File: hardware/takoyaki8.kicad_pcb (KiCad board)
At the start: 2 copper layers, 0 parts

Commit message: Place parts on first-draft layout: outline with RP2040-Zero notch, mounting holes, OLED silk outline removed (DRC clean except silk text)
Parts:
- added C1: 100nF, Capacitor_SMD:C_0603_1608Metric, B.Cu at (133.5, 85.8)
- added C2: 100nF, Capacitor_SMD:C_0603_1608Metric, B.Cu at (152.6, 85.8)
- added C3: 100nF, Capacitor_SMD:C_0603_1608Metric, B.Cu at (171.6, 85.8)
- added C4: 100nF, Capacitor_SMD:C_0603_1608Metric, B.Cu at (190.7, 85.8)
- added D1: 1N4148W, Diode_SMD:D_SOD-123, B.Cu at (140.5, 75.5)
- added D2: 1N4148W, Diode_SMD:D_SOD-123, B.Cu at (159.6, 75.5)
- added D3: 1N4148W, Diode_SMD:D_SOD-123, B.Cu at (178.6, 75.5)
- added D4: 1N4148W, Diode_SMD:D_SOD-123, B.Cu at (197.7, 75.5)
- added D5: 1N4148W, Diode_SMD:D_SOD-123, B.Cu at (140.5, 94.5)
- added D6: 1N4148W, Diode_SMD:D_SOD-123, B.Cu at (159.6, 94.5)
- added D7: 1N4148W, Diode_SMD:D_SOD-123, B.Cu at (178.6, 94.5)
- added D8: 1N4148W, Diode_SMD:D_SOD-123, B.Cu at (197.7, 94.5)
- added J1: OLED_0.91in, takoyaki8:OLED_0.91in_I2C_Header, F.Cu at (117.4, 97.2)
- added LED1: WS2812B, LED_SMD:LED_WS2812B_PLCC4_5.0x5.0mm_P3.2mm, B.Cu at (133.5, 82.0)
- added LED2: WS2812B, LED_SMD:LED_WS2812B_PLCC4_5.0x5.0mm_P3.2mm, B.Cu at (152.6, 82.0)
- added LED3: WS2812B, LED_SMD:LED_WS2812B_PLCC4_5.0x5.0mm_P3.2mm, B.Cu at (171.6, 82.0)
- added LED4: WS2812B, LED_SMD:LED_WS2812B_PLCC4_5.0x5.0mm_P3.2mm, B.Cu at (190.7, 82.0)
- added R1: 0R, Resistor_SMD:R_0603_1608Metric, B.Cu at (128.0, 80.3)
- added SW1: SW_Push, takoyaki8:SW_choc_v2_HS_CPG135001S30_1u, B.Cu at (133.5, 70.5)
- added SW2: SW_Push, takoyaki8:SW_choc_v2_HS_CPG135001S30_1u, B.Cu at (152.6, 70.5)
- added SW3: SW_Push, takoyaki8:SW_choc_v2_HS_CPG135001S30_1u, B.Cu at (171.6, 70.5)
- added SW4: SW_Push, takoyaki8:SW_choc_v2_HS_CPG135001S30_1u, B.Cu at (190.7, 70.5)
- added SW5: SW_Push, takoyaki8:SW_choc_v2_HS_CPG135001S30_1u, B.Cu at (133.5, 89.5)
- added SW6: SW_Push, takoyaki8:SW_choc_v2_HS_CPG135001S30_1u, B.Cu at (152.6, 89.5)
- added SW7: SW_Push, takoyaki8:SW_choc_v2_HS_CPG135001S30_1u, B.Cu at (171.6, 89.5)
- added SW8: SW_Push, takoyaki8:SW_choc_v2_HS_CPG135001S30_1u, B.Cu at (190.7, 89.5)
- added U1: RP2040-Zero, takoyaki8:RP2040-Zero_Castellated_Flipped, F.Cu at (113.6, 71.9)
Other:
- board outline added: 99.9 x 40 mm

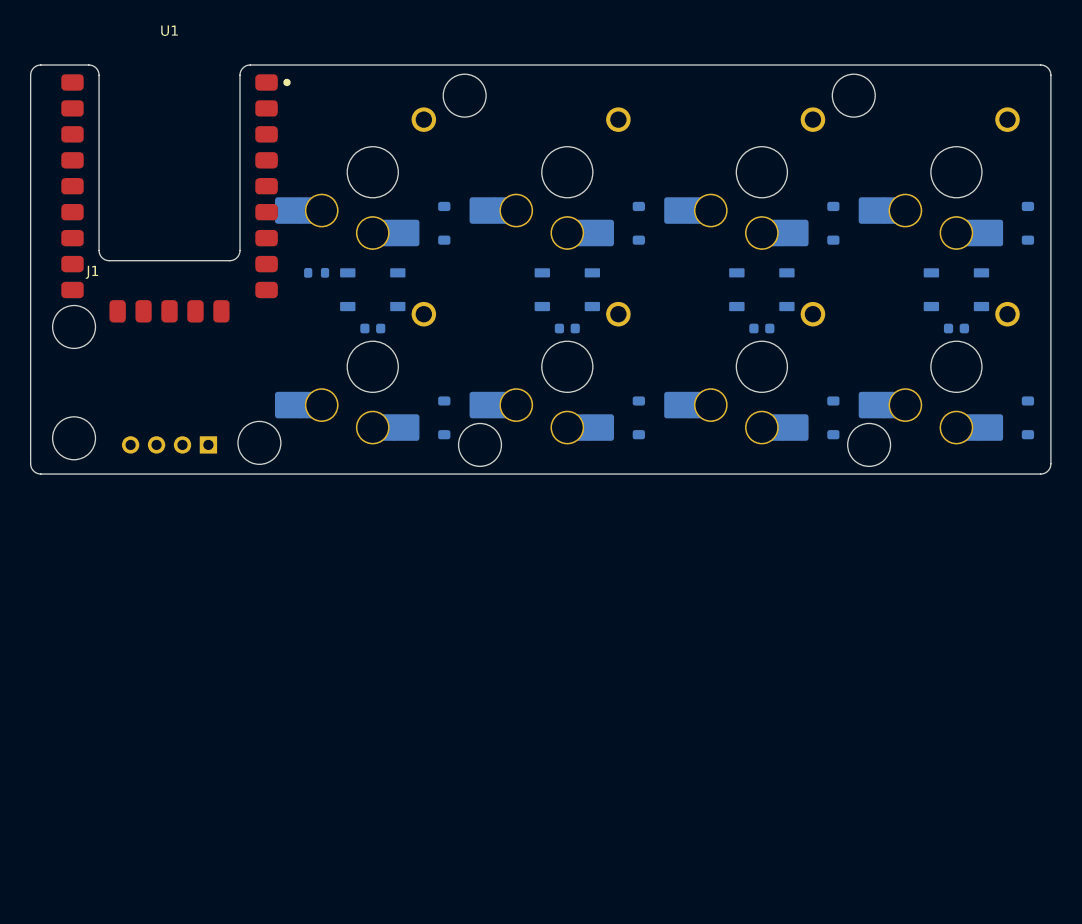
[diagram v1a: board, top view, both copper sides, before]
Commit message: Add top plate, panel tabs and mouse-bite holes (DRC clean except silk text)
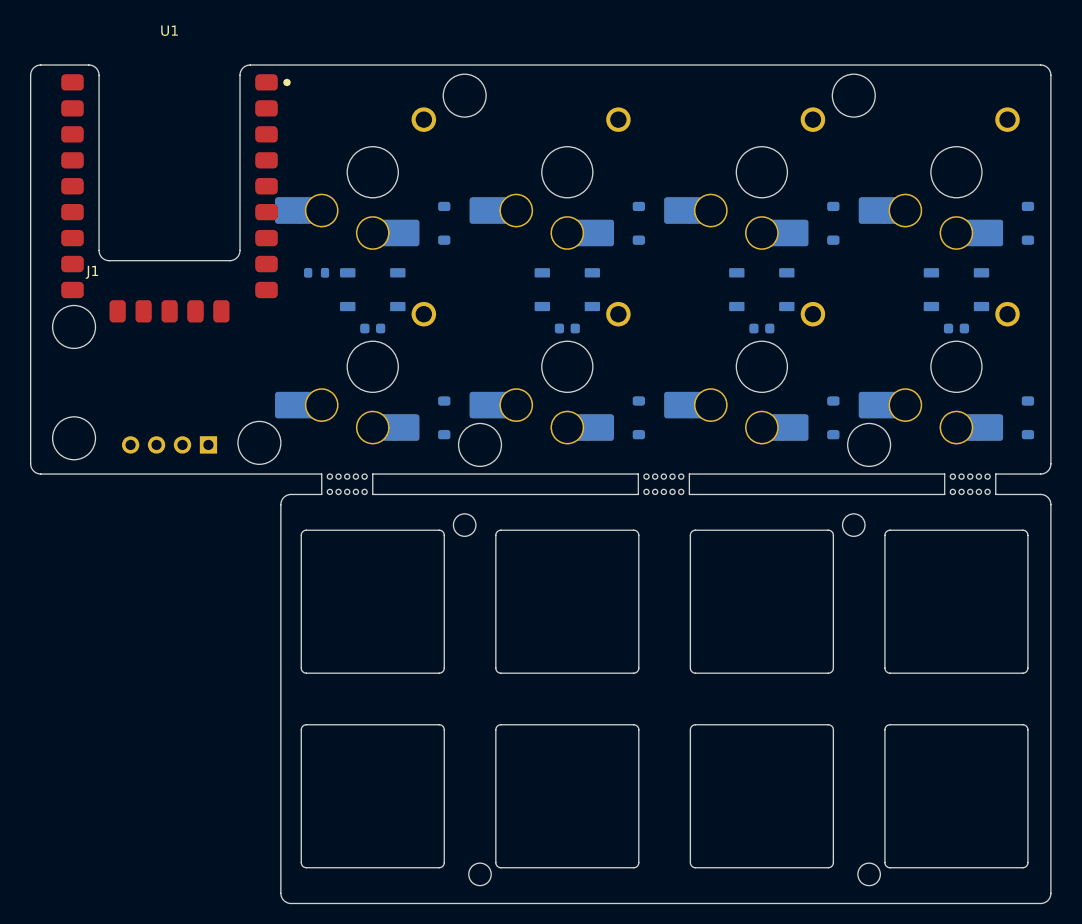
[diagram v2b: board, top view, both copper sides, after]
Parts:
- added MB1: MouseBite, takoyaki8:MouseBite_5x0.5mm_P0.85mm, F.Cu at (131.0, 100.3)
- added MB2: MouseBite, takoyaki8:MouseBite_5x0.5mm_P0.85mm, F.Cu at (131.0, 101.8)
- added MB3: MouseBite, takoyaki8:MouseBite_5x0.5mm_P0.85mm, F.Cu at (162.0, 100.3)
- added MB4: MouseBite, takoyaki8:MouseBite_5x0.5mm_P0.85mm, F.Cu at (162.0, 101.8)
- added MB5: MouseBite, takoyaki8:MouseBite_5x0.5mm_P0.85mm, F.Cu at (192.0, 100.3)
- added MB6: MouseBite, takoyaki8:MouseBite_5x0.5mm_P0.85mm, F.Cu at (192.0, 101.8)
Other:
- board size 99.9 x 40 mm -> 99.9 x 82.1 mm

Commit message: Add GND zones on both layers, Power netclass, hole-to-hole 0.5mm (DRC: 0 errors, 40 unconnected, 24 mouse-bite hole warnings)
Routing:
- added copper zone on B.Cu, net GND
- added copper zone on F.Cu, net GND
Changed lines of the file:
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@@
 		(capping no)
 		(filling no)
+		(zone_defaults)
 		(pcbplotparams
 			(layerselection 0x00000000_00000000_55555555_5755f5ff)
@@
 		(layer "Edge.Cuts")
 	)
+	(zone
+		(net "GND")
+		(layers "F.Cu" "B.Cu")
+		(hatch edge 0.5)
+		(connect_pads
+			(clearance 0.2)
+		)
+		(min_thickness 0.25)
+		(fill yes
+			(thermal_gap 0.3)
+			(thermal_bridge_width 0.4)
+			(island_removal_mode 0)
+		)
+		(polygon
+			(pts
+				(xy 99.05 59) (xy 200.95 59) (xy 200.9 99.55) (xy 99 99.55)
+			)
+		)
+	)
 	(embedded_fonts no)

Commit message: Route +5V: U1 to LEDs and bypass caps (DRC: 0 errors, 32 unconnected)
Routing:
- net +5V: track 0.00 -> 121.2 mm, vias 0 -> 1
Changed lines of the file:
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@@
 		)
+	)
+	(segment
+		(start 123.1 61.71)
+		(end 126 61.71)
+		(width 0.5)
+		(layer "F.Cu")
+		(net "+5V")
+	)
+	(segment
+		(start 126 61.71)
+		(end 126 79)
+		(width 0.5)
+		(layer "F.Cu")
+		(net "+5V")
+	)
+	(segment
+		(start 126 79)
+		(end 135.95 79)
+		(width 0.5)
+		(layer "B.Cu")
+		(net "+5V")
+	)
+	(segment
+		(start 135.95 79)
+		(end 155 79)
+		(width 0.5)
+		(layer "B.Cu")
+		(net "+5V")
+	)
+	(segment
+		(start 155 79)
+		(end 174.05 79)
+		(width 0.5)
+		(layer "B.Cu")
+		(net "+5V")
+	)
+	(segment
+		(start 174.05 79)
+		(end 193.1 79)
+		(width 0.5)
+		(layer "B.Cu")
+		(net "+5V")
+	)
+	(segment
+		(start 135.95 79)
+		(end 135.95 80.35)
+		(width 0.5)
+		(layer "B.Cu")
+		(net "+5V")
+	)
+	(segment
+		(start 155 79)
+		(end 155 80.35)
+		(width 0.5)
+		(layer "B.Cu")
+		(net "+5V")
+	)
+	(segment
+		(start 174.05 79)
+		(end 174.05 80.35)
+		(width 0.5)
+		(layer "B.Cu")
+		(net "+5V")
+	)
+	(segment
+		(start 193.1 79)
+		(end 193.1 80.35)
+		(width 0.5)
+		(layer "B.Cu")
+		(net "+5V")
+	)
+	(segment
+		(start 134.275 85.8)
+		(end 134.275 80.35)
+		(width 0.5)
+		(layer "B.Cu")
+		(net "+5V")
+	)
+	(segment
+		(start 134.275 80.35)
+		(end 135.95 80.35)
+		(width 0.5)
+		(layer "B.Cu")
+		(net "+5V")
+	)
+	(segment
+		(start 153.325 85.8)
+		(end 153.325 80.35)
+		(width 0.5)
+		(layer "B.Cu")
+		(net "+5V")
+	)
+	(segment
+		(start 153.325 80.35)
+		(end 155 80.35)
+		(width 0.5)
+		(layer "B.Cu")
+		(net "+5V")
+	)
+	(segment
+		(start 172.375 85.8)
+		(end 172.375 80.35)
+		(width 0.5)
+		(layer "B.Cu")
+		(net "+5V")
+	)
+	(segment
+		(start 172.375 80.35)
+		(end 174.05 80.35)
+		(width 0.5)
+		(layer "B.Cu")
+		(net "+5V")
+	)
+	(segment
+		(start 191.425 85.8)
+		(end 191.425 80.35)
+		(width 0.5)
+		(layer "B.Cu")
+		(net "+5V")
+	)
+	(segment
+		(start 191.425 80.35)
+		(end 193.1 80.35)
+		(width 0.5)
+		(layer "B.Cu")
+		(net "+5V")
+	)
+	(via
+		(at 126 79)
+		(size 0.6)
+		(drill 0.3)
+		(layers "F.Cu" "B.Cu")
+		(net "+5V")
 	)
 	(embedded_fonts no)

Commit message: Route LED data chain (GPIO26 -> R1 -> LED1..4) and chamfer +5V corners (DRC: 0 errors, 27 unconnected)
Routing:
- net LED_D1: track 0.00 -> 16.9 mm
- net LED_D2: track 0.00 -> 16.9 mm
- net LED_D3: track 0.00 -> 16.9 mm
- net LED_DATA: track 0.00 -> 7.18 mm, vias 0 -> 1
- net Net-(LED1-DIN): track 0.00 -> 2.23 mm
- net +5V: track 121.2 -> 119.7 mm
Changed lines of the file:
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@@
 		(capping no)
 		(filling no)
-		(zone_defaults)
 		(pcbplotparams
 			(layerselection 0x00000000_00000000_55555555_5755f5ff)
@@
 		(layer "Edge.Cuts")
 	)
-	(zone
-		(net "GND")
-		(layers "F.Cu" "B.Cu")
-		(hatch edge 0.5)
-		(connect_pads
-			(clearance 0.2)
-		)
-		(min_thickness 0.25)
-		(fill yes
-			(thermal_gap 0.3)
-			(thermal_bridge_width 0.4)
-			(island_removal_mode 0)
-		)
-		(polygon
-			(pts
-				(xy 99.05 59) (xy 200.95 59) (xy 200.9 99.55) (xy 99 99.55)
-			)
-		)
+	(segment
+		(start 126 62.21)
+		(end 126 79)
+		(width 0.5)
+		(layer "F.Cu")
+		(net "+5V")
 	)
 	(segment
-		(start 123.1 61.71)
-		(end 126 61.71)
+		(start 125.5 61.71)
+		(end 126 62.21)
 		(width 0.5)
 		(layer "F.Cu")
@@
 	)
 	(segment
-		(start 126 61.71)
-		(end 126 79)
+		(start 123.1 61.71)
+		(end 125.5 61.71)
 		(width 0.5)
 		(layer "F.Cu")
 		(net "+5V")
 	)
+	(via
+		(at 126 79)
+		(size 0.6)
+		(drill 0.3)
+		(layers "F.Cu" "B.Cu")
+		(net "+5V")
+	)
+	(segment
+		(start 134.775 80.35)
+		(end 135.95 80.35)
+		(width 0.5)
+		(layer "B.Cu")
+		(net "+5V")
+	)
+	(segment
+		(start 191.925 80.35)
+		(end 193.1 80.35)
+		(width 0.5)
+		(layer "B.Cu")
+		(net "+5V")
+	)
+	(segment
+		(start 153.325 80.85)
+		(end 153.825 80.35)
+		(width 0.5)
+		(layer "B.Cu")
+		(net "+5V")
+	)
 	(segment
 		(start 126 79)
@@
 	)
 	(segment
-		(start 135.95 79)
-		(end 155 79)
+		(start 153.825 80.35)
+		(end 155 80.35)
 		(width 0.5)
 		(layer "B.Cu")
@@
 	)
 	(segment
-		(start 155 79)
-		(end 174.05 79)
+		(start 193.1 79)
+		(end 193.1 80.35)
 		(width 0.5)
 		(layer "B.Cu")
@@
 	)
 	(segment
-		(start 174.05 79)
-		(end 193.1 79)
+		(start 172.375 85.8)
+		(end 172.375 80.85)
+		(width 0.5)
+		(layer "B.Cu")
+		(net "+5V")
+	)
+	(segment
+		(start 172.375 80.85)
+		(end 172.875 80.35)
 		(width 0.5)
 		(layer "B.Cu")
@@
 	)
 	(segment
-		(start 155 79)
-		(end 155 80.35)
+		(start 172.875 80.35)
+		(end 174.05 80.35)
+		(width 0.5)
+		(layer "B.Cu")
+		(net "+5V")
+	)
+	(segment
+		(start 191.425 85.8)
+		(end 191.425 80.85)
 		(width 0.5)
 		(layer "B.Cu")
@@
 	)
 	(segment
-		(start 193.1 79)
-		(end 193.1 80.35)
+		(start 135.95 79)
+		(end 155 79)
 		(width 0.5)
 		(layer "B.Cu")
@@
 	(segment
 		(start 134.275 85.8)
-		(end 134.275 80.35)
+		(end 134.275 80.85)
 		(width 0.5)
 		(layer "B.Cu")
@@
 	)
 	(segment
-		(start 134.275 80.35)
-		(end 135.95 80.35)
+		(start 134.275 80.85)
+		(end 134.775 80.35)
 		(width 0.5)
 		(layer "B.Cu")
@@
 	(segment
 		(start 153.325 85.8)
-		(end 153.325 80.35)
+		(end 153.325 80.85)
 		(width 0.5)
 		(layer "B.Cu")
@@
 	)
 	(segment
-		(start 153.325 80.35)
+		(start 155 79)
 		(end 155 80.35)
 		(width 0.5)
@@
 	)
 	(segment
-		(start 172.375 85.8)
-		(end 172.375 80.35)
+		(start 191.425 80.85)
+		(end 191.925 80.35)
 		(width 0.5)
 		(layer "B.Cu")
@@
 	)
 	(segment
-		(start 172.375 80.35)
-		(end 174.05 80.35)
+		(start 174.05 79)
+		(end 193.1 79)
 		(width 0.5)
 		(layer "B.Cu")
@@
 	)
 	(segment
-		(start 191.425 85.8)
-		(end 191.425 80.35)
+		(start 155 79)
+		(end 174.05 79)
 		(width 0.5)
 		(layer "B.Cu")
@@
 	)
 	(segment
-		(start 191.425 80.35)
-		(end 193.1 80.35)
-		(width 0.5)
-		(layer "B.Cu")
-		(net "+5V")
+		(start 123.1 76.95)
+		(end 125 76.95)
+		(width 0.25)
+		(layer "F.Cu")
+		(net "LED_DATA")
 	)
 	(via
-		(at 126 79)
+		(at 125 76.95)
 		(size 0.6)
 		(drill 0.3)
 		(layers "F.Cu" "B.Cu")
-		(net "+5V")
+		(net "LED_DATA")
+	)
+	(segment
+		(start 125 76.95)
+		(end 125 79.85)
+		(width 0.25)
+		(layer "B.Cu")
+		(net "LED_DATA")
+	)
+	(segment
+		(start 125 79.85)
+		(end 125.5 80.35)
+		(width 0.25)
+		(layer "B.Cu")
+		(net "LED_DATA")
+	)
+	(segment
+		(start 125.5 80.35)
+		(end 127.175 80.35)
+		(width 0.25)
+		(layer "B.Cu")
+		(net "LED_DATA")
+	)
+	(segment
+		(start 174.05 83.65)
+		(end 174.05 82.5)
+		(width 0.25)
+		(layer "B.Cu")
+		(net "LED_D3")
+	)
+	(segment
+		(start 187.7 82)
+		(end 188.2 81.5)
+		(width 0.25)
+		(layer "B.Cu")
+		(net "LED_D3")
+	)
+	(segment
+		(start 188.2 81.5)
+		(end 188.2 80.35)
+		(width 0.25)
+		(layer "B.Cu")
+		(net "LED_D3")
+	)
+	(segment
+		(start 174.05 82.5)
+		(end 174.55 82)
+		(width 0.25)
+		(layer "B.Cu")
+		(net "LED_D3")
+	)
+	(segment
+		(start 174.55 82)
+		(end 187.7 82)
+		(width 0.25)
+		(layer "B.Cu")
+		(net "LED_D3")
+	)
+	(segment
+		(start 168.65 82)
+		(end 169.15 81.5)
+		(width 0.25)
+		(layer "B.Cu")
+		(net "LED_D2")
+	)
+	(segment
+		(start 169.15 81.5)
+		(end 169.15 80.35)
+		(width 0.25)
+		(layer "B.Cu")
+		(net "LED_D2")
+	)
+	(segment
+		(start 155 83.65)
+		(end 155 82.5)
+		(width 0.25)
+		(layer "B.Cu")
+		(net "LED_D2")
+	)
+	(segment
+		(start 155.5 82)
+		(end 168.65 82)
+		(width 0.25)
+		(layer "B.Cu")
+		(net "LED_D2")
+	)
+	(segment
+		(start 155 82.5)
+		(end 155.5 82)
+		(width 0.25)
+		(layer "B.Cu")
+		(net "LED_D2")
+	)
+	(segment
+		(start 135.95 83.65)
+		(end 135.95 82.5)
+		(width 0.25)
+		(layer "B.Cu")
+		(net "LED_D1")
+	)
+	(segment
+		(start 149.6 82)
+		(end 150.1 81.5)
+		(width 0.25)
+		(layer "B.Cu")
+		(net "LED_D1")
+	)
+	(segment
+		(start 150.1 81.5)
+		(end 150.1 80.35)
+		(width 0.25)
+		(layer "B.Cu")
+		(net "LED_D1")
+	)
+	(segment
+		(start 135.95 82.5)
+		(end 136.45 82)
+		(width 0.25)
+		(layer "B.Cu")
+		(net "LED_D1")
+	)
+	(segment
+		(start 136.45 82)
+		(end 149.6 82)
+		(width 0.25)
+		(layer "B.Cu")
+		(net "LED_D1")
+	)
+	(segment
+		(start 128.825 80.35)
+		(end 131.05 80.35)
+		(width 0.25)
+		(layer "B.Cu")
+		(net "Net-(LED1-DIN)")
+	)
+	(zone
+		(net "GND")
+		(layers "F.Cu" "B.Cu")
+		(hatch edge 0.5)
+		(connect_pads
+			(clearance 0.2)
+		)
+		(min_thickness 0.25)
+		(fill yes
+			(thermal_gap 0.3)
+			(thermal_bridge_width 0.4)
+			(island_removal_mode 0)
+		)
+		(polygon
+			(pts
+				(xy 99.05 59) (xy 200.95 59) (xy 200.9 99.55) (xy 99 99.55)
+			)
+		)
 	)
 	(embedded_fonts no)

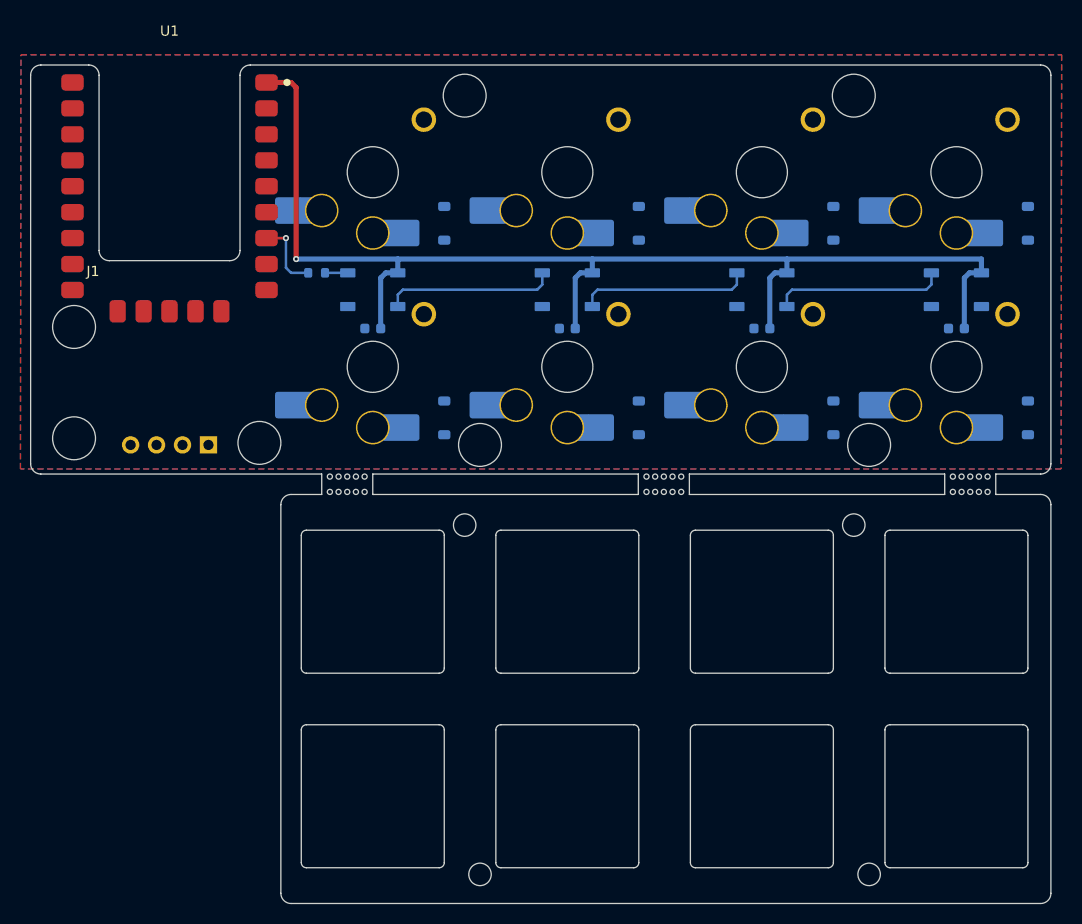
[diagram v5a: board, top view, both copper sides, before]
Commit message: Route matrix, I2C and +3V3 by hand, add GND stitching vias (DRC: 0 errors, 0 unconnected, 48 warnings: mouse-bite holes and silk)
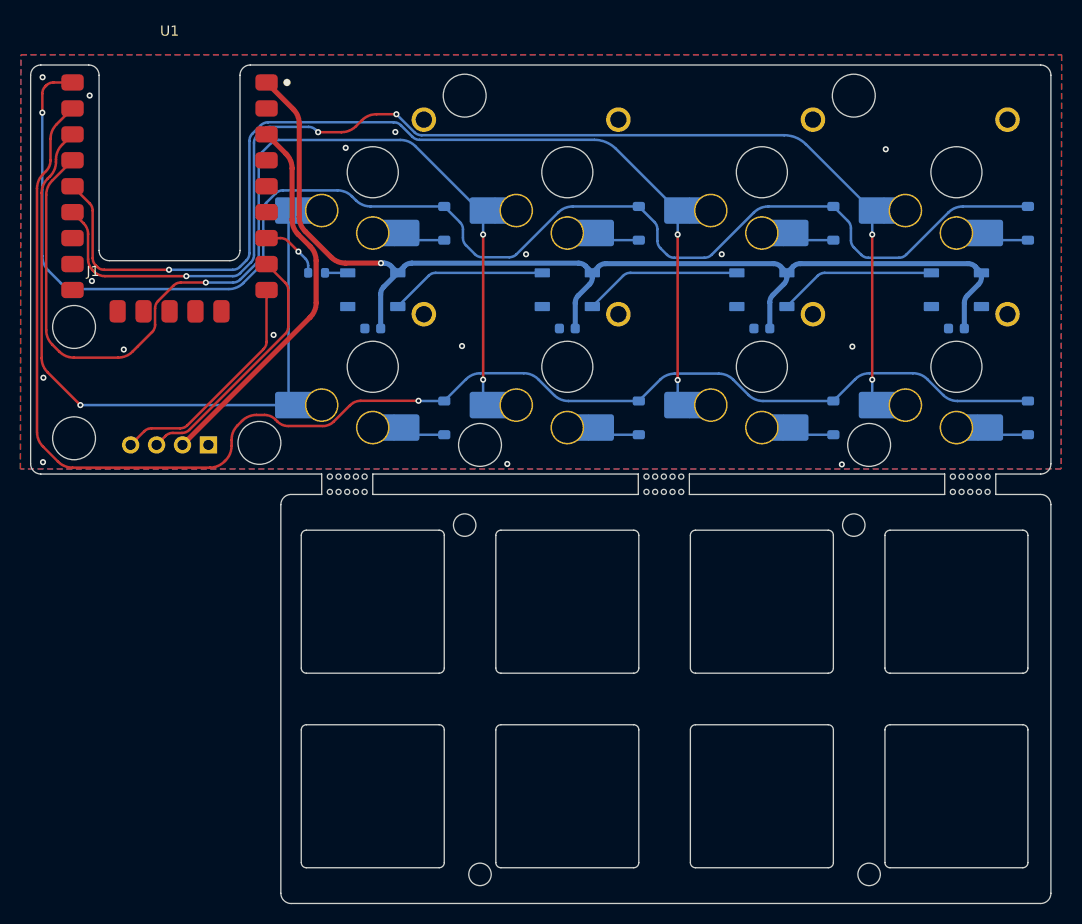
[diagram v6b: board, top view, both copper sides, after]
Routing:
- net ROW1: track 0.00 -> 141.8 mm, vias 0 -> 1
- net ROW0: track 0.00 -> 140.0 mm, vias 0 -> 1
- net COL3: track 0.00 -> 119.1 mm, vias 0 -> 5
- net COL2: track 0.00 -> 100.8 mm, vias 0 -> 3
- net COL1: track 0.00 -> 99.5 mm, vias 0 -> 3
- net COL0: track 0.00 -> 68.4 mm, vias 0 -> 1
- net +3V3: track 0.00 -> 37.5 mm
- net I2C_SCL: track 0.00 -> 24.8 mm
- net I2C_SDA: track 0.00 -> 22.7 mm
- net +5V: track 119.7 -> 109.9 mm
- net Net-(D6-A): track 0.00 -> 4.04 mm
- net Net-(D2-A): track 0.00 -> 4.04 mm
- net Net-(D8-A): track 0.00 -> 4.04 mm
- net Net-(D7-A): track 0.00 -> 4.04 mm
- net Net-(D5-A): track 0.00 -> 4.04 mm
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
